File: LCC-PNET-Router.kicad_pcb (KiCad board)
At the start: 2 copper layers, 63.5 x 119.4 mm, 40 parts, among them J101 USB_A, J201 Termination, J202 RJ45, J203 RJ45, J301 Termination, J302 PNET, J303 PNET, P1 POCKETBEAGLE-P1, P2 POCKETBEAGLE-P2, T201 LCC Power Out, T202 LCC Power In, U201 LM358, U202 TCAN332DR, U301 LM358, U302 TCAN332DR, U401 LM2574N-5.0

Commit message: Completed initial HW design.
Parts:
- removed D401: SB160-E3/54, Diodes_THT:D_DO-41_SOD81_P7.62mm_Horizontal
- added C403: 22uf, Capacitors_SMD:C_0603, F.Cu at (114.3, 102.1)
- added C404: 22uf, Capacitors_SMD:C_0603, F.Cu at (112.4, 102.1)
- added REF**: MountingHole_3.2mm_M3, Mounting_Holes:MountingHole_3.2mm_M3, F.Cu at (113.0, 153.7)
- added REF**: MountingHole_3.2mm_M3, Mounting_Holes:MountingHole_3.2mm_M3, F.Cu at (168.9, 153.7)
- added REF**: MountingHole_3.2mm_M3, Mounting_Holes:MountingHole_3.2mm_M3, F.Cu at (168.9, 41.9)
- added REF**: MountingHole_3.2mm_M3, Mounting_Holes:MountingHole_3.2mm_M3, F.Cu at (113.0, 41.9)
- C201, C202, C301, C302: footprint Capacitors_THT:C_Rect_L4.0mm_W2.5mm_P2.50mm -> Capacitors_SMD:C_0603
- C203, C303: footprint Capacitors_THT:CP_Radial_D6.3mm_P2.50mm -> Capacitors_SMD:CP_Elec_4x5.8
- C401: value 220 uf 25V -> 10uf; footprint Capacitors_THT:CP_Radial_D8.0mm_P3.50mm -> Capacitors_SMD:CP_Elec_5x5.3
- C402: value 22 uf 100V -> 100nf; footprint Capacitors_THT:CP_Radial_D8.0mm_P3.50mm -> Capacitors_SMD:C_0603
- D201: value CAN Tx -> LCC Tx; footprint LEDs:LED_D3.0mm -> LEDs:LED_0603
- D202: value CAN Rx -> LCC Rx; footprint LEDs:LED_D3.0mm -> LEDs:LED_0603
- D203, D204: footprint Diodes_THT:D_DO-15_P10.16mm_Horizontal -> Diodes_SMD:D_PowerDI-123
- D301: value CAN Tx -> PNET Tx; footprint LEDs:LED_D3.0mm -> LEDs:LED_0603
- D302: value CAN Rx -> PNET Rx; footprint LEDs:LED_D3.0mm -> LEDs:LED_0603
- L401: value 330 uh -> 4.7uH; footprint PELowProfile:PE-LowProfile -> Inductors_SMD:L_7.3x7.3_H4.5
- R201, R202, R301, R302: footprint Resistors_THT:R_Axial_DIN0204_L3.6mm_D1.6mm_P1.90mm_Vertical -> Resistors_SMD:R_0603
- R203, R204, R303, R304: footprint Resistors_THT:R_Axial_DIN0204_L3.6mm_D1.6mm_P2.54mm_Vertical -> Resistors_SMD:R_1206
- U201, U301: footprint Housings_DIP:DIP-8_W7.62mm -> Housings_SOIC:SOIC-8_3.9x4.9mm_Pitch1.27mm
- U202, U302: footprint Housings_SOIC:SOIC-8-1EP_3.9x4.9mm_Pitch1.27mm -> Housings_SOIC:SOIC-8_3.9x4.9mm_Pitch1.27mm
- U401: value LM2574N-5.0 -> AP63205; footprint Housings_DIP:DIP-8_W7.62mm -> TO_SOT_Packages_SMD:TSOT-23-6_MK06A
- moved C402 57.3 mm to (121.9, 103.4), turned to 270 degrees
- moved C401 51.1 mm to (119.1, 97.2), turned to 0 degrees
- moved L401 49.3 mm to (118.7, 110.5)
- moved U401 47.6 mm to (118.2, 103.8)
- moved D301 40.4 mm to (122.4, 134.6), turned to 180 degrees
- moved D302 40.4 mm to (122.4, 139.7), turned to 180 degrees
- moved R302 32.3 mm to (126.2, 139.7), turned to 0 degrees
- moved R301 32.1 mm to (126.2, 134.6), turned to 0 degrees
- moved C303 20.8 mm to (143.0, 128.3), turned to 0 degrees
- moved C203 15.3 mm to (137.7, 81.3), turned to 180 degrees
- moved C301 13.7 mm to (143.0, 132.1), turned to 0 degrees
- moved R203 10.5 mm to (143.9, 49.5), turned to 180 degrees
- moved R304 10.1 mm to (144.6, 147.3), turned to 180 degrees
- moved U301 9.53 mm to (132.7, 137.3)
- moved D202 9.13 mm to (159.2, 68.6)
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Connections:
- C301 pad 1: Net-(C301-Pad1) -> +3V3
- C303 pad 1: Net-(C301-Pad1) -> +3V3
- C401 pad 1: +5V -> /CAN_12V
- C402 pad 1: /CAN_12V -> Net-(C402-Pad1)
- C402 pad 2: GND -> Net-(C402-Pad2)
- L401 pad 1: Net-(D401-Pad1) -> +5V
- L401 pad 2: +5V -> Net-(C402-Pad2)
- U401 pad 2: GND -> /CAN_12V
- U401 pad 3: GND -> /CAN_12V
- U401 pad 5: /CAN_12V -> Net-(C402-Pad2)
- U401 pad 6: (no net) -> Net-(C402-Pad1)
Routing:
- net /CAN_12V: track 0.00 -> 128.9 mm, vias 0 -> 5
- net /CAN1_RX: track 0.00 -> 70.3 mm, vias 0 -> 3
- net /CAN0_RX: track 0.00 -> 66.7 mm, vias 0 -> 3
- net /CAN1_TX: track 0.00 -> 58.8 mm, vias 0 -> 1
- net Net-(J202-Pad1): track 0.00 -> 58.1 mm, vias 0 -> 2
- net Net-(J302-Pad6): track 0.00 -> 57.9 mm, vias 0 -> 2
- net /CAN0_TX: track 0.00 -> 57.3 mm, vias 0 -> 3
- net Net-(J202-Pad2): track 0.00 -> 53.7 mm, vias 0 -> 3
- net Net-(J302-Pad3): track 0.00 -> 50.0 mm, vias 0 -> 4
- net Net-(J302-Pad1): track 0.00 -> 46.6 mm, vias 0 -> 2
- net Net-(J302-Pad4): track 0.00 -> 43.5 mm, vias 0 -> 3
- net Net-(J202-Pad5): track 0.00 -> 34.1 mm
- net GND: track 0.00 -> 33.3 mm, vias 0 -> 9
- net Net-(J202-Pad4): track 0.00 -> 28.0 mm
- net Net-(J101-Pad3): track 0.00 -> 9.78 mm
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- added copper zone on F.Cu, net +5V
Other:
- net class Default: clearance 0.254 -> 0.2; trace_width 0.254 -> 0.25; via_dia 0.889 -> 0.6; via_drill 0.635 -> 0.4
- rule trace_clearance: 0.254 -> 0.2
- rule trace_min: 0.254 -> 0.25
- rule via_min_drill: 0.508 -> 0.4
- rule via_min_size: 0.889 -> 0.6

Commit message: Completed initial HW design.
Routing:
- net /CAN0_RX: track 66.7 -> 68.9 mm, vias 3 -> 4
- net /CAN1_TX: track 58.8 -> 61.0 mm, vias 1 -> 3
- net /CAN1_RX: track 70.3 -> 69.9 mm, vias 3 -> 4
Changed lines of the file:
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@@
     (thickness 1.6)
     (drawings 4)
-    (tracks 240)
+    (tracks 237)
     (zones 0)
     (modules 45)
@@
   )
   (setup
-    (last_trace_width 0.5)
+    (last_trace_width 0.25)
     (user_trace_width 0.5)
     (trace_clearance 0.2)
@@
   (segment (start 142.24 140.02) (end 142.24 143.51) (width 0.25) (layer F.Cu) (net 26))
   (via (at 142.24 143.51) (size 0.6) (drill 0.4) (layers F.Cu B.Cu) (net 26))
+  (segment (start 133.97501 76.91999) (end 133.97501 111.335736) (width 0.25) (layer F.Cu) (net 47))
+  (segment (start 135.89 75.005) (end 133.97501 76.91999) (width 0.25) (layer F.Cu) (net 47))
+  (segment (start 135.89 73.98) (end 135.89 75.005) (width 0.25) (layer F.Cu) (net 47))
+  (via (at 133.97501 111.76) (size 0.6) (drill 0.4) (layers F.Cu B.Cu) (net 47))
+  (segment (start 133.97501 111.335736) (end 133.97501 111.76) (width 0.25) (layer F.Cu) (net 47))
+  (segment (start 129.54 111.76) (end 133.97501 111.76) (width 0.25) (layer B.Cu) (net 47))
   (segment (start 147.32 72.39) (end 147.32 73.98) (width 0.25) (layer F.Cu) (net 47))
   (segment (start 135.89 72.39) (end 147.32 72.39) (width 0.25) (layer B.Cu) (net 47))
@@
   (segment (start 135.89 73.98) (end 135.89 72.39) (width 0.25) (layer F.Cu) (net 47))
   (via (at 135.89 72.39) (size 0.6) (drill 0.4) (layers F.Cu B.Cu) (net 47))
-  (segment (start 133.35 111.76) (end 129.54 111.76) (width 0.25) (layer B.Cu) (net 47))
-  (segment (start 135.89 73.98) (end 135.89 75.005) (width 0.25) (layer F.Cu) (net 47))
-  (segment (start 135.89 75.005) (end 133.35 77.545) (width 0.25) (layer F.Cu) (net 47))
-  (segment (start 133.35 77.545) (end 133.35 80.38859) (width 0.25) (layer F.Cu) (net 47))
-  (segment (start 133.35 80.38859) (end 133.35 111.76) (width 0.25) (layer F.Cu) (net 47))
-  (via (at 133.35 111.76) (size 0.6) (drill 0.4) (layers F.Cu B.Cu) (net 47))
+  (segment (start 133.355002 69.855002) (end 133.35 69.85) (width 0.25) (layer B.Cu) (net 49))
+  (segment (start 139.7 69.855002) (end 133.355002 69.855002) (width 0.25) (layer B.Cu) (net 49))
+  (segment (start 133.35 114.3) (end 133.35 69.85) (width 0.25) (layer F.Cu) (net 49))
+  (via (at 133.35 69.85) (size 0.6) (drill 0.4) (layers F.Cu B.Cu) (net 49))
+  (segment (start 129.54 114.3) (end 133.35 114.3) (width 0.25) (layer B.Cu) (net 49))
+  (via (at 133.35 114.3) (size 0.6) (drill 0.4) (layers F.Cu B.Cu) (net 49))
   (segment (start 139.7 69.855002) (end 139.7 73.98) (width 0.25) (layer F.Cu) (net 49))
   (segment (start 148.59 69.85) (end 139.705002 69.85) (width 0.25) (layer B.Cu) (net 49))
@@
   (segment (start 148.59 68.58) (end 148.59 69.85) (width 0.25) (layer F.Cu) (net 49))
   (via (at 148.59 69.85) (size 0.6) (drill 0.4) (layers F.Cu B.Cu) (net 49))
-  (segment (start 140.97 114.3) (end 129.54 114.3) (width 0.25) (layer B.Cu) (net 49))
-  (segment (start 139.7 73.98) (end 139.7 75.005) (width 0.25) (layer F.Cu) (net 49))
-  (segment (start 139.7 75.005) (end 141.115001 76.420001) (width 0.25) (layer F.Cu) (net 49))
-  (segment (start 141.115001 76.420001) (end 141.115001 114.154999) (width 0.25) (layer F.Cu) (net 49))
-  (segment (start 141.115001 114.154999) (end 140.97 114.3) (width 0.25) (layer F.Cu) (net 49))
-  (via (at 140.97 114.3) (size 0.6) (drill 0.4) (layers F.Cu B.Cu) (net 49))
-  (segment (start 133.975001 133.584999) (end 133.975001 138.369999) (width 0.25) (layer F.Cu) (net 66))
-  (segment (start 133.975001 138.369999) (end 133.35 138.995) (width 0.25) (layer F.Cu) (net 66))
-  (segment (start 133.35 138.995) (end 133.35 140.02) (width 0.25) (layer F.Cu) (net 66))
-  (segment (start 134.112 132.08) (end 134.112 133.448) (width 0.25) (layer F.Cu) (net 66))
-  (segment (start 134.112 133.448) (end 133.975001 133.584999) (width 0.25) (layer F.Cu) (net 66))
-  (segment (start 139.554999 132.179999) (end 134.211999 132.179999) (width 0.25) (layer B.Cu) (net 66))
-  (segment (start 134.211999 132.179999) (end 134.112 132.08) (width 0.25) (layer B.Cu) (net 66))
-  (via (at 134.112 132.08) (size 0.6) (drill 0.4) (layers F.Cu B.Cu) (net 66))
-  (via (at 139.554999 132.179999) (size 0.6) (drill 0.4) (layers F.Cu B.Cu) (net 66))
-  (segment (start 139.7 91.44) (end 152.4 91.44) (width 0.25) (layer B.Cu) (net 66))
-  (segment (start 140.97 134.62) (end 140.97 133.595) (width 0.25) (layer F.Cu) (net 66))
-  (segment (start 139.554999 132.179999) (end 139.554999 91.585001) (width 0.25) (layer F.Cu) (net 66))
-  (segment (start 140.97 133.595) (end 139.554999 132.179999) (width 0.25) (layer F.Cu) (net 66))
-  (segment (start 139.554999 91.585001) (end 139.7 91.44) (width 0.25) (layer F.Cu) (net 66))
-  (via (at 139.7 91.44) (size 0.6) (drill 0.4) (layers F.Cu B.Cu) (net 66))
+  (segment (start 147.066 91.44) (end 147.066 136.906) (width 0.25) (layer F.Cu) (net 66))
+  (segment (start 140.97 136.906) (end 147.066 136.906) (width 0.25) (layer B.Cu) (net 66))
+  (via (at 147.066 136.906) (size 0.6) (drill 0.4) (layers F.Cu B.Cu) (net 66))
+  (segment (start 152.4 91.44) (end 147.066 91.44) (width 0.25) (layer B.Cu) (net 66))
+  (via (at 147.066 91.44) (size 0.6) (drill 0.4) (layers F.Cu B.Cu) (net 66))
+  (segment (start 133.35 140.02) (end 133.35 136.906) (width 0.25) (layer F.Cu) (net 66))
+  (segment (start 140.97 136.906) (end 133.35 136.906) (width 0.25) (layer B.Cu) (net 66))
+  (via (at 133.35 136.906) (size 0.6) (drill 0.4) (layers F.Cu B.Cu) (net 66))
+  (segment (start 140.97 136.906) (end 140.97 134.62) (width 0.25) (layer F.Cu) (net 66))
+  (via (at 140.97 136.906) (size 0.6) (drill 0.4) (layers F.Cu B.Cu) (net 66))
+  (segment (start 134.874 136.144) (end 134.874 134.874) (width 0.25) (layer F.Cu) (net 68))
+  (segment (start 134.874 134.874) (end 134.62 134.62) (width 0.25) (layer F.Cu) (net 68))
+  (segment (start 144.78 136.144) (end 134.874 136.144) (width 0.25) (layer B.Cu) (net 68))
+  (via (at 134.874 136.144) (size 0.6) (drill 0.4) (layers F.Cu B.Cu) (net 68))
+  (segment (start 144.78 134.62) (end 144.78 136.144) (width 0.25) (layer F.Cu) (net 68))
+  (via (at 144.78 136.144) (size 0.6) (drill 0.4) (layers F.Cu B.Cu) (net 68))
   (segment (start 146.304 93.98) (end 152.4 93.98) (width 0.25) (layer B.Cu) (net 68))
   (segment (start 144.78 134.62) (end 144.78 133.595) (width 0.25) (layer F.Cu) (net 68))
@@
   (segment (start 146.405001 94.081001) (end 146.304 93.98) (width 0.25) (layer F.Cu) (net 68))
   (via (at 146.304 93.98) (size 0.6) (drill 0.4) (layers F.Cu B.Cu) (net 68))
-  (segment (start 134.62 134.62) (end 135.17 134.62) (width 0.25) (layer F.Cu) (net 68))
-  (segment (start 135.17 134.62) (end 136.270001 135.720001) (width 0.25) (layer F.Cu) (net 68))
-  (segment (start 136.270001 135.720001) (end 144.154999 135.720001) (width 0.25) (layer F.Cu) (net 68))
-  (segment (start 144.154999 135.720001) (end 144.78 135.095) (width 0.25) (layer F.Cu) (net 68))
   (segment (start 144.78 135.095) (end 144.78 134.62) (width 0.25) (layer F.Cu) (net 68))
   (segment (start 149.86 73.98) (end 148.59 73.98) (width 0.25) (layer F.Cu) (net 91))
@@
     (polygon
       (pts
-        (xy 109.22 38.1) (xy 128.27 38.1) (xy 128.27 128.27) (xy 109.22 128.27)
+        (xy 109.22 38.1) (xy 127.762 38.1) (xy 127.762 128.27) (xy 109.22 128.27)
       )
     )
@@
     (polygon
       (pts
-        (xy 172.72 38.1) (xy 129.54 38.1) (xy 129.54 97.79) (xy 129.54 129.54) (xy 109.22 129.54)
-        (xy 109.22 157.48) (xy 172.72 157.48)
+        (xy 172.72 38.1) (xy 128.778 38.1) (xy 128.778 129.54) (xy 109.22 129.54) (xy 109.22 157.48)
+        (xy 172.72 157.48)
       )
     )

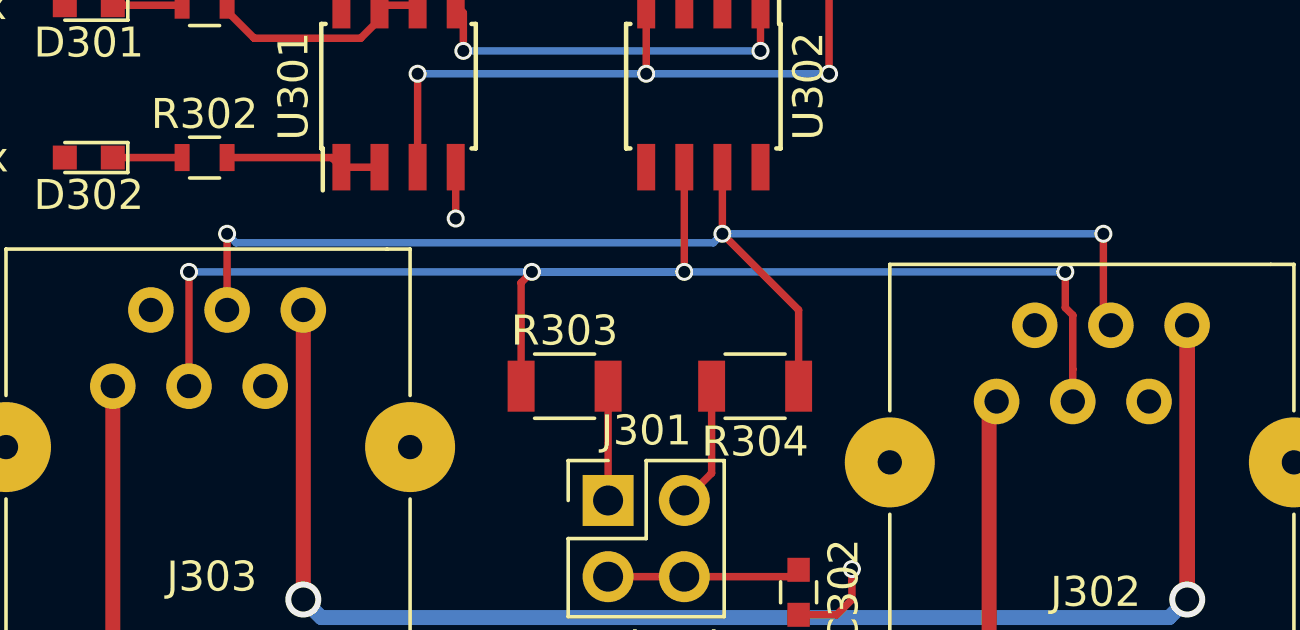
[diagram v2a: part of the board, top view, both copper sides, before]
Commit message: Correct for CAN Polarity on the PNET connectors.
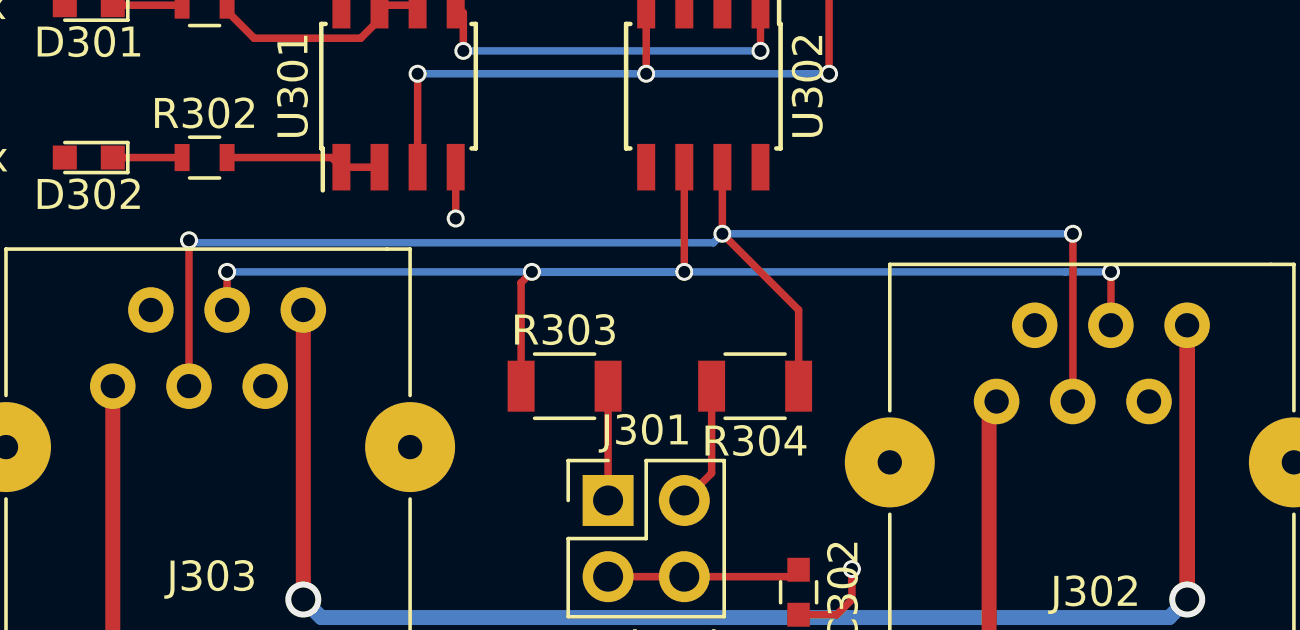
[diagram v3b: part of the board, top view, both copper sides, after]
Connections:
- J302 pad 3: Net-(J302-Pad3) -> /PNET CAN Transceiver/CAN-H
- J302 pad 4: Net-(J302-Pad4) -> /PNET CAN Transceiver/CAN-L
- J303 pad 3: Net-(J302-Pad3) -> /PNET CAN Transceiver/CAN-H
- J303 pad 4: Net-(J302-Pad4) -> /PNET CAN Transceiver/CAN-L
- R303 pad 1: Net-(J302-Pad3) -> /PNET CAN Transceiver/CAN-L
- R304 pad 1: Net-(J302-Pad4) -> /PNET CAN Transceiver/CAN-H
- U302 pad 6: Net-(J302-Pad3) -> /PNET CAN Transceiver/CAN-L
- U302 pad 7: Net-(J302-Pad4) -> /PNET CAN Transceiver/CAN-H
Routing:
- net Net-(J302-Pad3): track 50.0 -> 0.00 mm, vias 4 -> 0
- net /PNET CAN Transceiver/CAN-H: track 0.00 -> 48.4 mm, vias 0 -> 3
- net /PNET CAN Transceiver/CAN-L: track 0.00 -> 45.4 mm, vias 0 -> 4
- net Net-(J302-Pad4): track 43.5 -> 0.00 mm, vias 3 -> 0

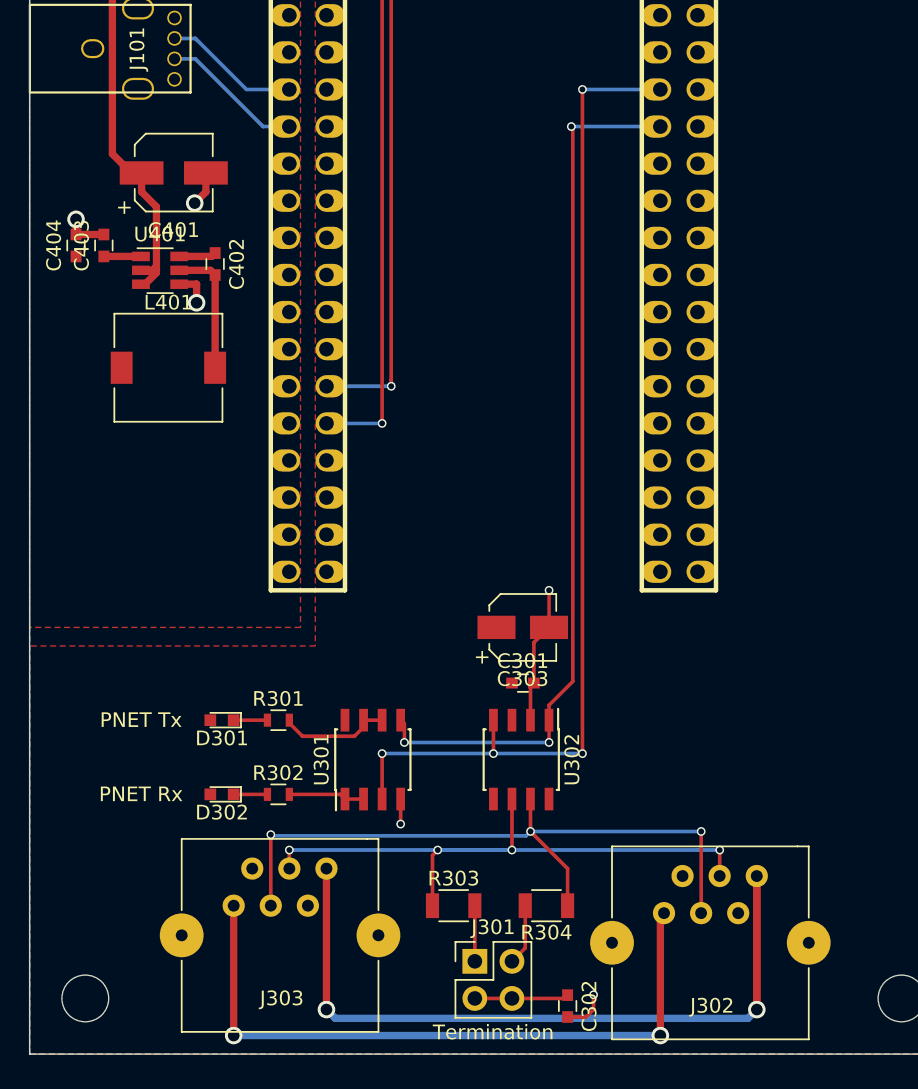
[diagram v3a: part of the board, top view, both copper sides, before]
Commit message: Update RJ12 Jacks.
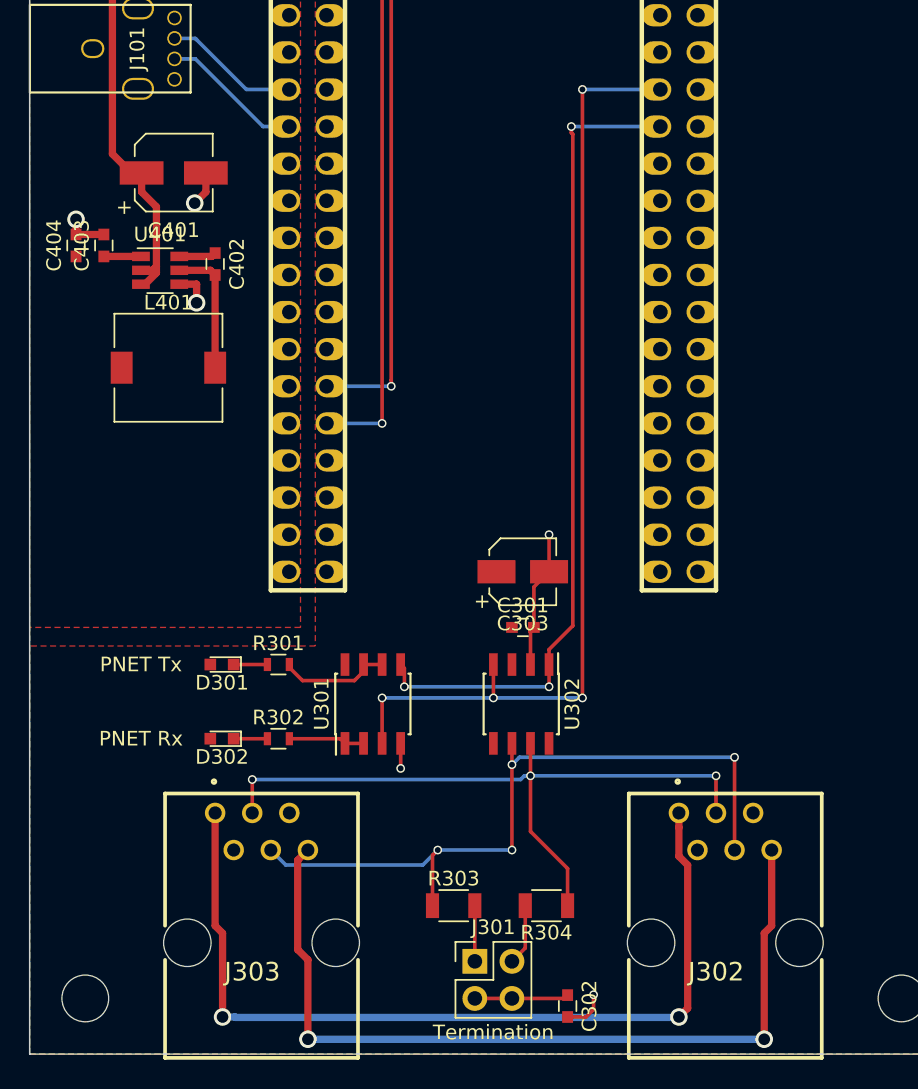
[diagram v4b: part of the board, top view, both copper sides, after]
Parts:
- J302, J303: footprint Connectors:RJ12_E -> RJ12Molex:95501-2661
- moved J302 9.49 mm to (161.9, 149.9)
- moved J303 7.43 mm to (130.2, 149.9)
- moved C303 3.81 mm to (143.0, 124.5)
- moved C301 3.81 mm to (143.0, 128.3)
- moved D301 3.81 mm to (122.4, 130.8)
- moved D302 3.81 mm to (122.4, 135.9)
- moved R301 3.81 mm to (126.2, 130.8)
- moved R302 3.81 mm to (126.2, 135.9)
- moved U301 3.81 mm to (132.7, 133.5)
- moved U302 3.81 mm to (142.9, 133.5)
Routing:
- net Net-(J302-Pad1): track 46.6 -> 59.9 mm
- net /PNET CAN Transceiver/CAN-L: track 45.4 -> 50.4 mm
- net /CAN1_RX: track 69.9 -> 66.1 mm
- net /CAN1_TX: track 61.0 -> 57.3 mm
